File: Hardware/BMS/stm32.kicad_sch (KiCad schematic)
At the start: 33 parts, among them J401 Conn_01x04_Socket, J402 USB_C_Receptacle_USB2.0_16P, Q401 2N7002E, SW401 SW_SPDT, SW402 SW_MEC_5G, U401 STM32G473CCTx, U402 TCAN1042VDRQ1, U403 USBLC6-2SC6, Y401 48 MHZ

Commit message: add stm layout
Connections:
- net SWCLK: now also J401.2 (Pin_2); no longer J401.3 (Pin_3)
- net SWDIO: now also J401.3 (Pin_3); no longer J401.2 (Pin_2)
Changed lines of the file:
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@@
+		)
+	)
+	(label "SWDIO"
+		(at 232.41 107.95 0)
+		(effects
+			(font
+				(size 1.27 1.27)
+			)
+			(justify left bottom)
 		)
 	)
@@
 		)
 	)
-	(label "SWCLK"
-		(at 232.41 107.95 0)
-		(effects
-			(font
-				(size 1.27 1.27)
-			)
-			(justify left bottom)
-		)
-	)
 	(label "VDDA"
 		(at 86.36 24.13 180)
@@
 		)
 	)
-	(label "SWDIO"
-		(at 232.41 105.41 0)
-		(effects
-			(font
-				(size 1.27 1.27)
-			)
-			(justify left bottom)
-		)
-	)
 	(label "SWCLK"
 		(at 102.87 69.85 180)
@@
 		)
 	)
+	(label "SWCLK"
+		(at 232.41 105.41 0)
+		(effects
+			(font
+				(size 1.27 1.27)
+			)
+			(justify left bottom)
+		)
+	)

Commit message: bms gotten to 0 unrouted traces!
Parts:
- removed Q401: 2N7002E, Package_TO_SOT_SMD:SOT-23, symbol Transistor_FET:2N7002E
- removed SW401: SW_SPDT, Button_Switch_SMD:SW_SPDT_Shouhan_MSK12C02, symbol Switch:SW_SPDT
- removed SW402: SW_MEC_5G, Button_Switch_SMD:SW_MEC_5GSH9, symbol Switch:SW_MEC_5G
- added Q401: DMN10H220L, Package_TO_SOT_SMD:SOT-23, symbol Transistor_FET:DMN10H220L
- added R409: 10k, Resistor_SMD:R_0603_1608Metric, symbol formula:R_10K
- added SW401, SW402: SW_Push, Button_Switch_SMD:SW_Push_1P1T_NO_CK_KMR2, symbol Switch:SW_Push
- J402: footprint Connector_USB:USB_C_Receptacle_G-Switch_GT-USB-7051x -> Connector_USB:USB_C_Receptacle_GCT_USB4105-xx-A_16P_TopMnt_Horizontal
- R401, R402: value 120 -> 60
- R403, R404: footprint footprints:R_0805_OEM -> Resistor_SMD:R_0603_1608Metric
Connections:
- net +3.3V: now also J401.1 (Pin_1), SW401.1
- net +5V: no longer J401.1 (Pin_1)
- net BMS_EN: now also Q401.3 (D)
- net BMS_HEARTBEAT: now also U401.46 (PB9); no longer U401.29 (PB15)
- net BMS_OK: now also U401.22 (PB10); no longer U401.39 (PA15)
- net CAN_COMS: now also U401.18 (PB2); no longer U401.44 (PB7)
- net DEBUG1: now also U401.40 (PB3); no longer U401.28 (PB14)
- net ERROR: now also U401.41 (PB4); no longer U401.42 (PB5)
- net GND: now also Q401.2 (S), R409.2, SW402.1
- net MUX1_COMS: now also U401.44 (PB7); no longer U401.46 (PB9)
- net MUX2_COMS: now also U401.39 (PA15); no longer U401.22 (PB10)
- net OT: now also U401.43 (PB6); no longer U401.40 (PB3)
- net OV: now also U401.29 (PB15); no longer U401.17 (PB1)
- net SWCLK: now also J401.3 (Pin_3); no longer J401.2 (Pin_2)
- net SWDIO: now also J401.2 (Pin_2); no longer J401.3 (Pin_3)
- net THERM_A2: now also U401.10 (PA2); no longer U401.9 (PA1)
- net THERM_B1: now also U401.9 (PA1); no longer U401.10 (PA2)
- net USB_C_COMS: now also U401.17 (PB1); no longer U401.43 (PB6)
- net UT: now also U401.42 (PB5); no longer U401.41 (PB4)
- net UV: now also U401.28 (PB14); no longer U401.18 (PB2)
- net at D401.2 (A), J402.A4 (VBUS), J402.A9 (VBUS)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: now also Q401.1 (G)
- net at C407.2, R403.1: now also R409.1, SW401.2
- net at C412.2, R404.2: now also SW402.2
- net FAN_INT: now reaches U401.2 (PC13)
- net FAN_EXT: now reaches U401.3 (PC14)
- no-connect marks 5 -> 3
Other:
- moved on the sheet: D401, R408

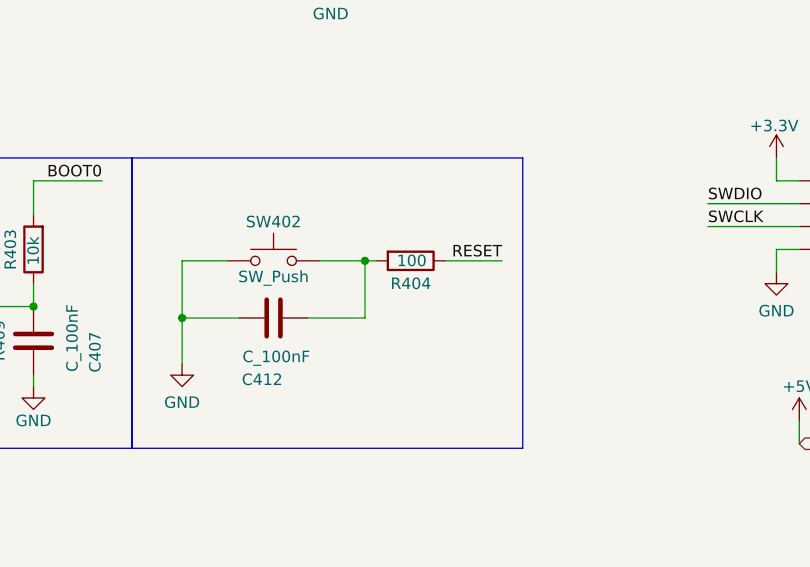
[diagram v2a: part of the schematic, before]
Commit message: fab updates to bms, power board, fet board
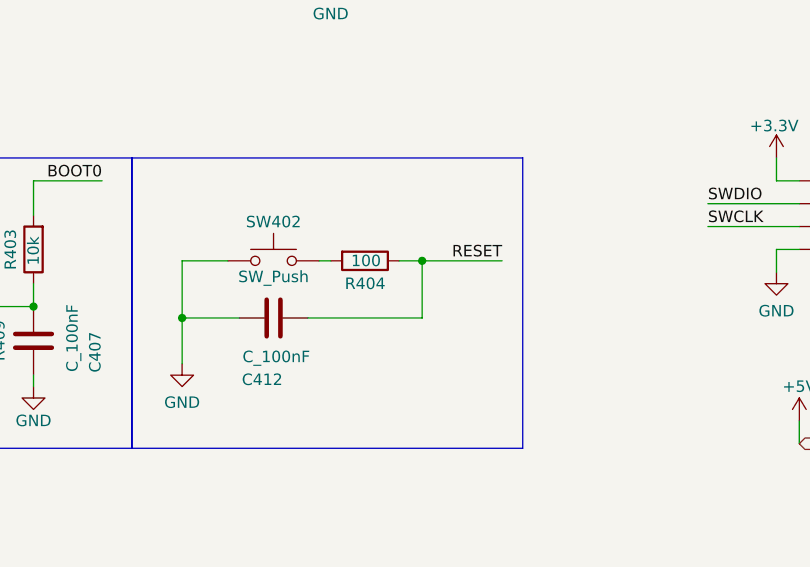
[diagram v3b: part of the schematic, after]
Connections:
- net RESET: now also C412.2
- net at R404.2, SW402.2: no longer C412.2
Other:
- moved on the sheet: R404
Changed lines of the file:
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@@
 	)
 	(junction
-		(at 194.31 111.76)
+		(at 81.28 172.72)
 		(diameter 0)
 		(color 0 0 0 0)
 	)
 	(junction
-		(at 81.28 172.72)
+		(at 247.65 40.64)
 		(diameter 0)
 		(color 0 0 0 0)
 	)
 	(junction
-		(at 247.65 40.64)
+		(at 200.66 111.76)
 		(diameter 0)
 		(color 0 0 0 0)
@@
 	(wire
 		(pts
+			(xy 200.66 111.76) (xy 209.55 111.76)
+		)
+		(stroke
+			(width 0)
+			(type default)
+		)
+	)
+	(wire
+		(pts
 			(xy 179.07 33.02) (xy 167.64 33.02)
 		)
@@
 		)
 	)
-	(wire
-		(pts
-			(xy 194.31 111.76) (xy 194.31 118.11)
-		)
-		(stroke
-			(width 0)
-			(type default)
-		)
-	)
-	(wire
-		(pts
-			(xy 195.58 111.76) (xy 194.31 111.76)
-		)
-		(stroke
-			(width 0)
-			(type default)
-		)
-	)
 	(polyline
 		(pts
@@
 	(wire
 		(pts
-			(xy 187.96 118.11) (xy 194.31 118.11)
+			(xy 187.96 118.11) (xy 200.66 118.11)
 		)
 		(stroke
@@
 	(wire
 		(pts
-			(xy 203.2 111.76) (xy 209.55 111.76)
-		)
-		(stroke
-			(width 0)
-			(type default)
-		)
-	)
-	(wire
-		(pts
 			(xy 69.85 21.59) (xy 69.85 26.67)
 		)
@@
 	(wire
 		(pts
-			(xy 189.23 111.76) (xy 194.31 111.76)
+			(xy 49.53 34.29) (xy 57.15 34.29)
 		)
 		(stroke
@@
 	(wire
 		(pts
-			(xy 49.53 34.29) (xy 57.15 34.29)
+			(xy 73.66 182.88) (xy 73.66 185.42)
 		)
 		(stroke
@@
 	(wire
 		(pts
-			(xy 73.66 182.88) (xy 73.66 185.42)
+			(xy 189.23 111.76) (xy 190.5 111.76)
 		)
 		(stroke
@@
 	(wire
 		(pts
+			(xy 200.66 111.76) (xy 198.12 111.76)
+		)
+		(stroke
+			(width 0)
+			(type default)
+		)
+	)
+	(wire
+		(pts
 			(xy 190.5 80.01) (xy 190.5 78.74)
 		)
@@
 	(wire
 		(pts
+			(xy 200.66 118.11) (xy 200.66 111.76)
+		)
+		(stroke
+			(width 0)
+			(type default)
+		)
+	)
+	(wire
+		(pts
 			(xy 54.61 50.8) (xy 54.61 46.99)
 		)
@@
 	(symbol
 		(lib_id "formula:R_10K")
-		(at 199.39 111.76 270)
+		(at 194.31 111.76 270)
 		(unit 1)
 		(exclude_from_sim no)
@@
 		(dnp no)
 		(property "Reference" "R404"
-			(at 201.676 114.3 90)
+			(at 196.596 114.3 90)
 			(effects
 				(font
@@
 		)
 		(property "Value" "100"
-			(at 201.168 111.76 90)
+			(at 196.088 111.76 90)
 			(effects
 				(font
@@
 		)
 		(property "Footprint" "Resistor_SMD:R_0603_1608Metric"
-			(at 199.39 109.982 0)
+			(at 194.31 109.982 0)
 			(effects
 				(font
@@
 		)
 		(property "Datasheet" "http://www.bourns.com/data/global/pdfs/CRS.pdf"
-			(at 199.39 113.792 0)
+			(at 194.31 113.792 0)
 			(effects
 				(font
@@
 		)
 		(property "Description" "Resistor, 10K, 0.25W, 1%, 0805"
-			(at 199.39 111.76 0)
+			(at 194.31 111.76 0)
 			(effects
 				(font
@@
 		)
 		(property "MFN" "DK"
-			(at 199.39 111.76 0)
+			(at 194.31 111.76 0)
 			(effects
 				(font
@@
 		)
 		(property "MPN" "CRS0805-FX-1002ELFCT-ND"
-			(at 199.39 111.76 0)
+			(at 194.31 111.76 0)
 			(effects
 				(font
@@
 		)
 		(property "PurchasingLink" "https://www.digikey.com/products/en?keywords=CRS0805-FX-1002ELFCT-ND"
-			(at 209.55 123.952 0)
+			(at 204.47 123.952 0)
 			(effects
 				(font
